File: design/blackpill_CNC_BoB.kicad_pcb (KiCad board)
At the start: 4 copper layers, 302 parts, among them J101 ALimIN, J102 ZLimIN, J103 YLimIN, J104 XLimIN, J105 CS_IN, J106 FH_IN, J107 DoorIN, J108 ResetIN, J109 ProbeIN, J110 12V Power in, J111 AuxEncIn, J112 5V Power out, J113 ADC_in_1, J114 ADC_in_2, J115 stepDriverLim, J116 Reset, J117 UART1, J118 I2C, J119 SpindleVFD, J120 Spindle/Coolant, J121 Spindle, J122 Coolant, J123 AuxOut, J124 XStepDrv, J125 YStepDrv, J126 ZStepDrv, J127 AStepDrv, J128 Driver Power in/out, J129 Relais Power in/out, U101 TLP290-4, U102 TLP290-4, U103 TLP290-4, U104 74LVC2G17, U105 LD1117S50TR_SOT223, U106 LM358, U107 TLV9001, U108 TLV9001, U109 YAAJ_WeAct_BlackPill_Part_Like, U110 TLV9001, U111 TLV9001, U112 74HCT541, U113 74HCT541, U114 74HCT541, U115 ULN2003A, U116 ULN2003A, U117 ULN2003A

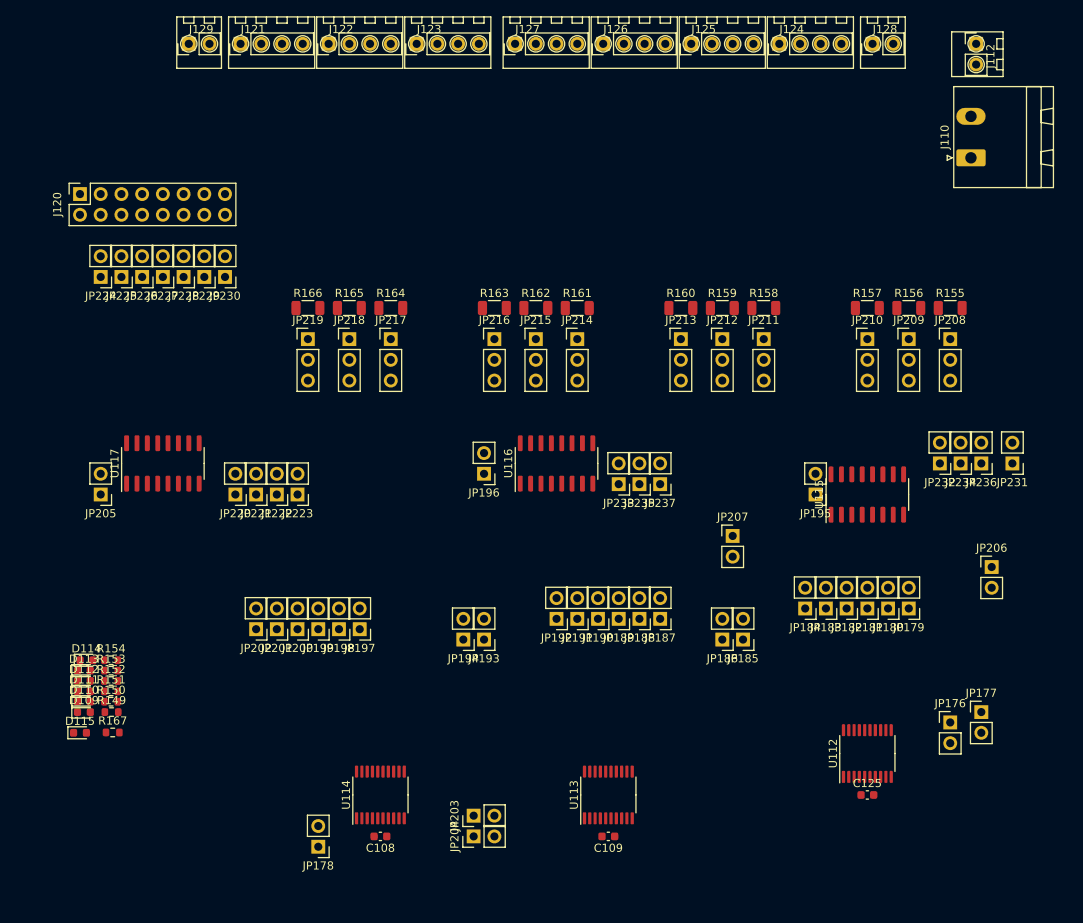
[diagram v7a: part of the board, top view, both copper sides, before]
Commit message: arranged output lines
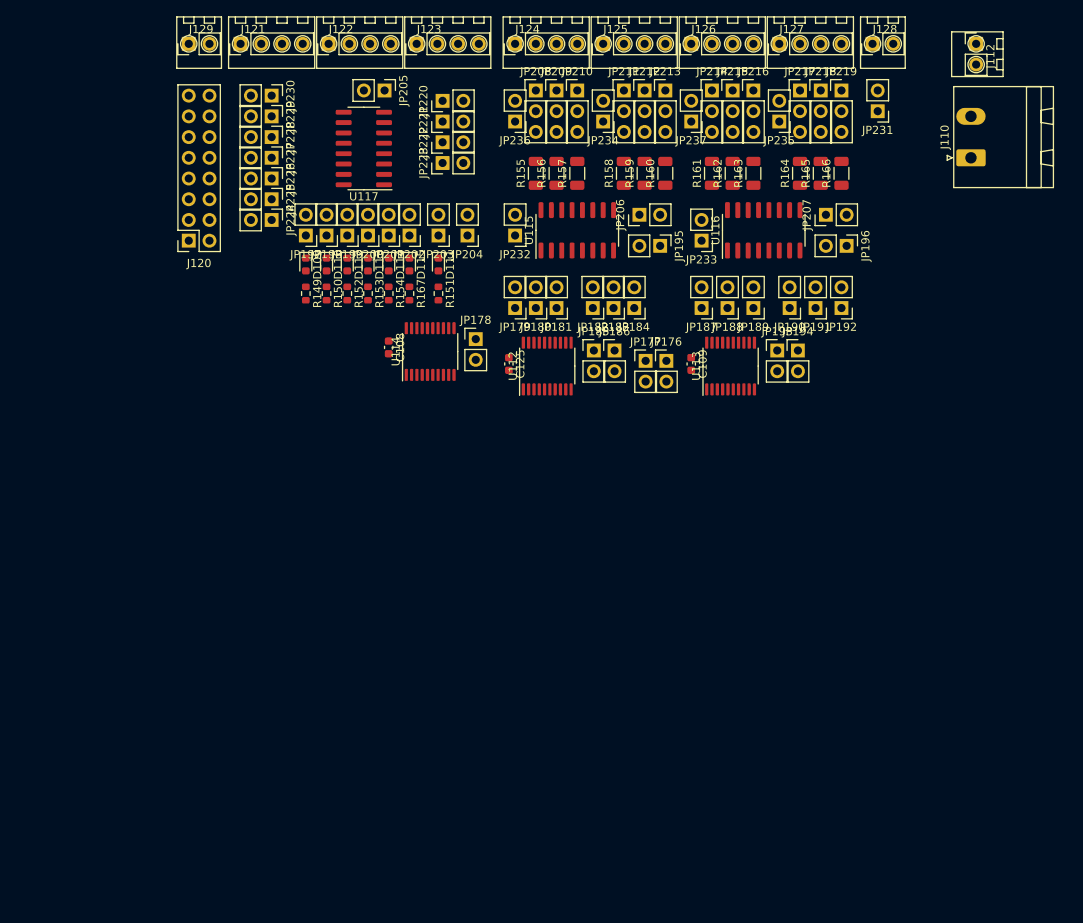
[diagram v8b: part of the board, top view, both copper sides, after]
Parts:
- moved JP204 73.7 mm to (36.1, 25.4), turned to 180 degrees
- moved JP219 72.2 mm to (81.9, 7.62)
- moved JP203 71.3 mm to (32.5, 25.4), turned to 180 degrees
- moved JP236 70.9 mm to (41.9, 11.4)
- moved D115 70.2 mm to (29.0, 29.0), turned to 270 degrees
- moved C125 68.7 mm to (41.1, 41.1), turned to 270 degrees
- moved D111 68.0 mm to (32.5, 29.0), turned to 270 degrees
- moved R166 67.5 mm to (81.9, 17.8), turned to 90 degrees
- moved JP218 65.3 mm to (79.4, 7.62)
- moved JP178 65.2 mm to (37.1, 38.1), turned to 0 degrees
- moved R167 65.0 mm to (29.0, 32.5), turned to 270 degrees
- moved R151 63.2 mm to (32.5, 32.5), turned to 270 degrees
- moved U112 61.6 mm to (45.8, 41.4)
- moved D110 61.3 mm to (18.8, 29.0), turned to 270 degrees
- moved D109 61.2 mm to (16.3, 29.0), turned to 270 degrees
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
